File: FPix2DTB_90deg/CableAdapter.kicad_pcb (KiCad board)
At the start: 2 copper layers, 40 x 40 mm, 4 parts, among them J1 CONN-SMK20, J2 CONN-SMK20

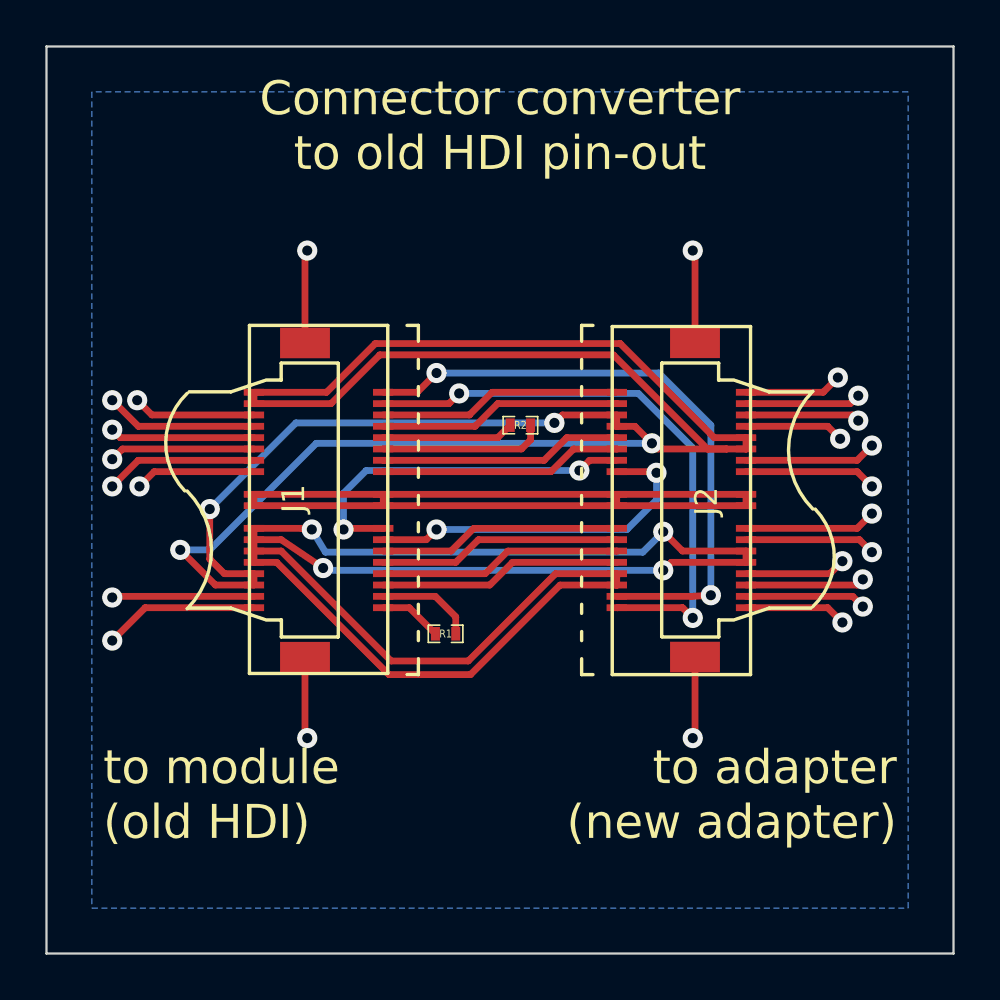
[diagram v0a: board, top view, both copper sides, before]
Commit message: Adjustments to silk screen
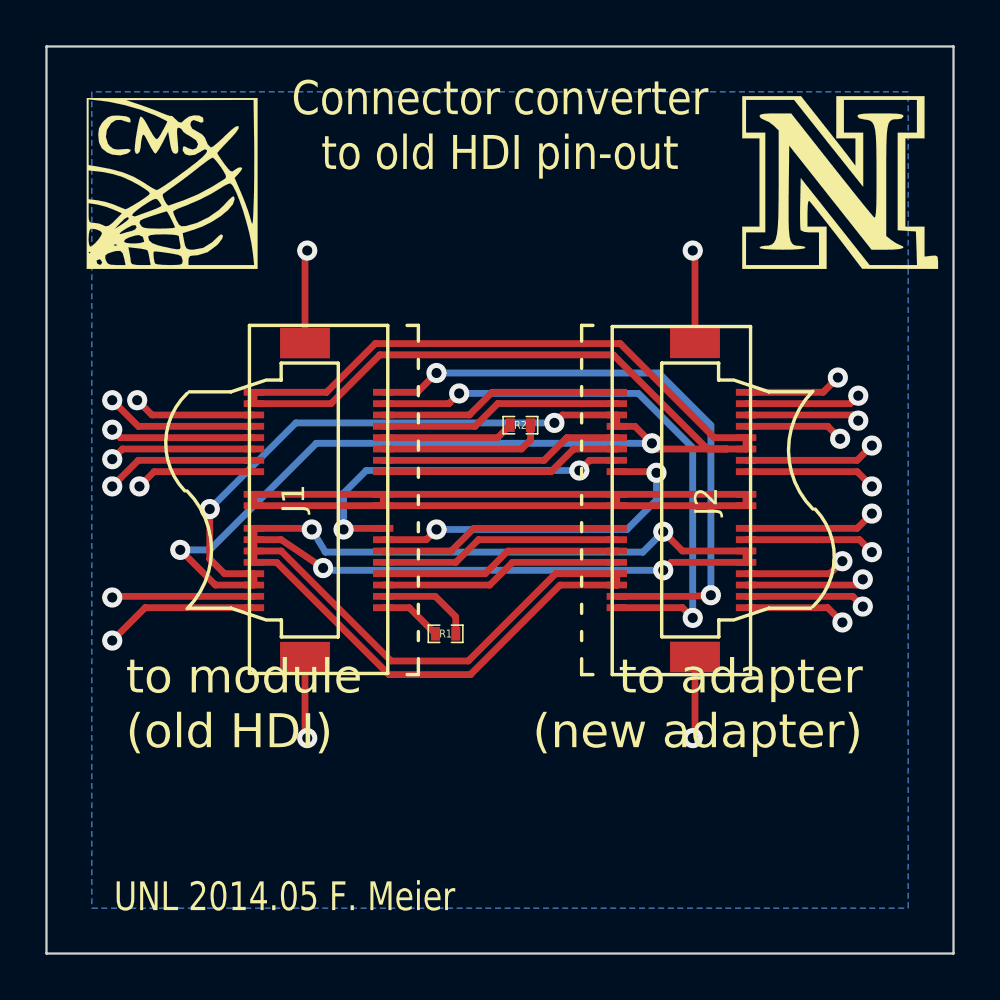
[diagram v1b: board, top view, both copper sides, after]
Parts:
- added G***: LOGO, LOGO, F.Cu at (101.0, 100.0)
- added G***: LOGOCMS, LOGOCMS, F.Cu at (71.5, 100.0)
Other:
- board text added: "UNL 2014.05 F. Meier"

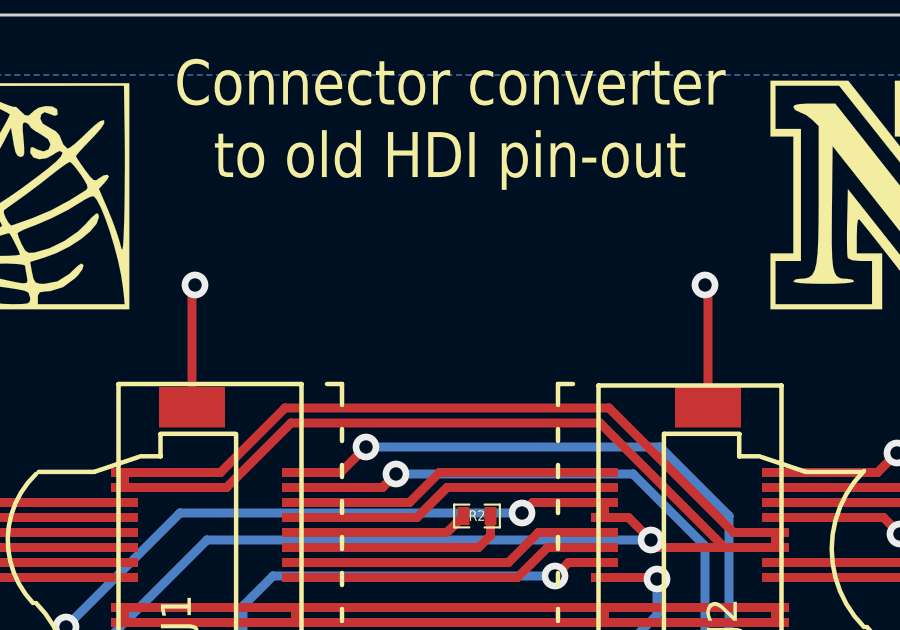
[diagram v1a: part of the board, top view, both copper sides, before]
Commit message: Added a mounting hole (maybe no one will ever use it but it is there)
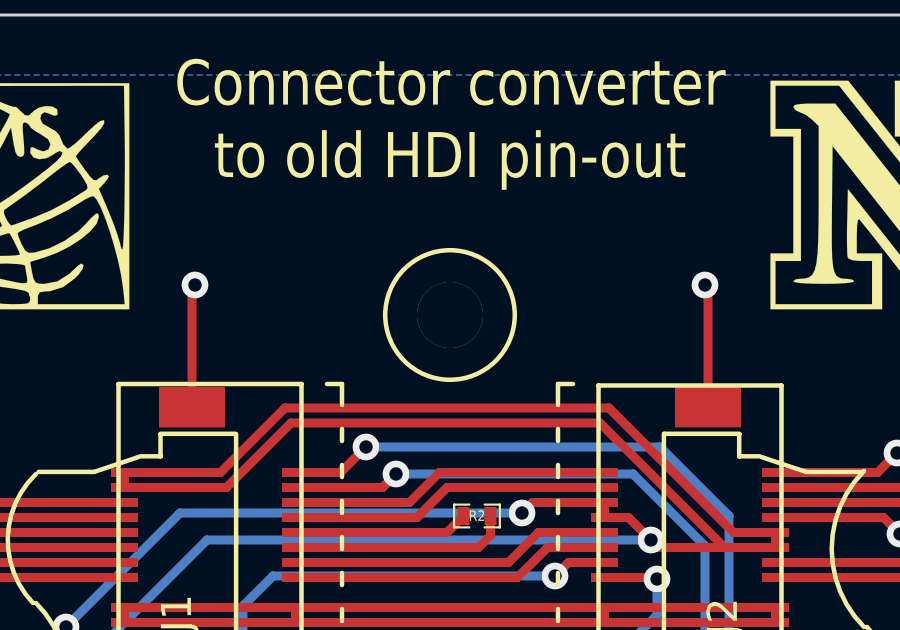
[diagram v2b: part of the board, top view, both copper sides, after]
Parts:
- added loch: M2, lochM2, F.Cu at (86.0, 104.0)
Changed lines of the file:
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@@
 (kicad_pcb (version 3) (host pcbnew "(2013-jul-07)-stable")
   (general
-    (links 0)
+    (links 60)
     (no_connects 0)
-    (area 65.949999 93.949999 106.050001 134.050001)
+    (area 65.222934 93.949999 106.050001 134.050001)
     (thickness 1.6)
     (drawings 8)
     (tracks 231)
     (zones 0)
-    (modules 6)
+    (modules 7)
     (nets 21)
   )
   (page A3)
+  (title_block
+    (title "Cable Adapter")
+    (rev 1)
+    (company "University of Nebraska-Lincoln")
+    (comment 1 "Adapter to use old HDI with new adapter board")
+  )
   (layers
     (15 F.Cu signal)
@@
     (visible_elements FFFFFBBF)
     (pcbplotparams
-      (layerselection 3178497)
+      (layerselection 2129921)
       (usegerberextensions true)
       (excludeedgelayer true)
@@
       (outputformat 1)
       (mirror false)
-      (drillshape 1)
+      (drillshape 0)
       (scaleselection 1)
       (outputdirectory ""))
@@
       (xy -1.78562 -1.44018)) (layer F.SilkS) (width 0.00254))
   )
+  (module lochM2 (layer F.Cu)
+    (at 86 104)
+    (fp_text reference loch (at 0.15 -0.5) (layer F.SilkS) hide
+      (effects (font (size 1 1) (thickness 0.15)))
+    )
+    (fp_text value M2 (at 0.05 0.9) (layer F.SilkS) hide
+      (effects (font (size 1 1) (thickness 0.15)))
+    )
+    (fp_circle (center 0 0) (end 1.6 -1.45) (layer F.SilkS) (width 0.15))
+    (pad 1 thru_hole circle (at 0 0) (size 2.2 2.2) (drill 2.2)
+      (layers *.Cu *.Mask F.SilkS)
+    )
+  )
   (gr_text "UNL 2014.05 F. Meier" (at 76.5 131.5) (layer F.SilkS)
